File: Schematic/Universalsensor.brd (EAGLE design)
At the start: 62 x 62.2 mm, 26 parts, among them IC1 MEGA328P-AU, IC2 DS18B20, IC3 DHT-22, IC4 SHT1X, IC5 MAX1724

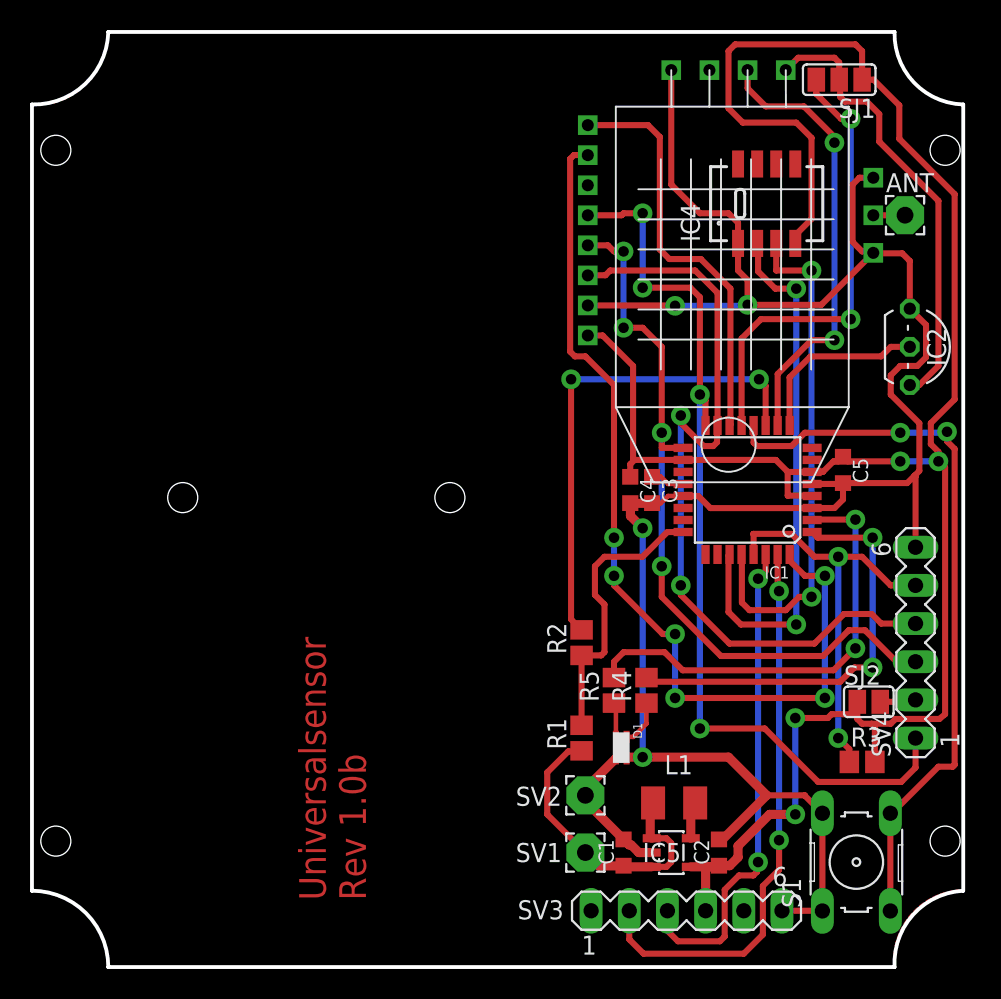
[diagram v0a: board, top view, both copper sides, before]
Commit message: new schematic for low freq crystal oscillator and sht21
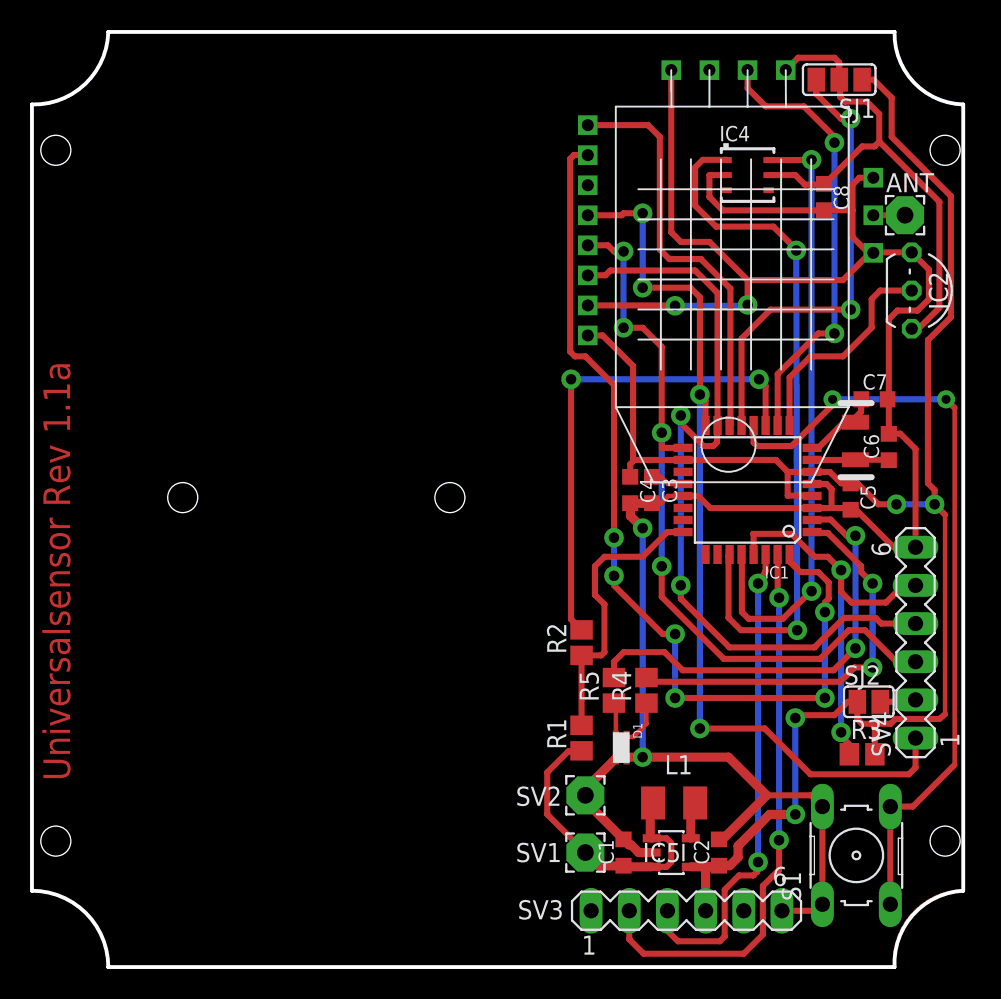
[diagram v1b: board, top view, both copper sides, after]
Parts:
- added C6, C7: 22pF, rcl:C0603K
- added C8: 100nF, rcl:C0603K
- added Q1: 32,768KHz, kanflo:OSCILLATOR_SMD
- IC4: value SHT1X -> SHT21; device sht10_11_15:SHT1X -> sensirion:DFN6/SHT
- moved IC2 3.75 mm to (58.5, 45.0)
- moved IC4 2.29 mm to (47.6, 52.7), turned to 270 degrees
- moved C5 1.85 mm to (54.5, 31.3)
- moved R3 0.51 mm to (55.2, 14.2)
- moved S1 0.44 mm to (54.9, 7.43)
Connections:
- new net N$3: C6.1, IC1.7, Q1.2
- new net N$8: C7.1, IC1.8, Q1.1
- net +3V3: no longer IC4.4
- net GND: now also C6.2, C7.2, C8.2, IC4.2; no longer IC4.1
- net SCL: now also IC4.6; no longer IC4.3
- net SDA: now also IC4.1; no longer IC4.2
- net U-SENS: now also C8.1, IC4.5
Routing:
- net +3V3: track 143.4 -> 114.4 mm
- net GND: track 149.9 -> 162.8 mm
- net SDA: track 36.0 -> 47.3 mm
- net SCL: track 34.3 -> 41.0 mm
- net N$8: track 0.00 -> 5.28 mm
- net N$3: track 0.00 -> 5.12 mm
- net U-SENS: track 30.2 -> 35.2 mm
- net D8: track 49.0 -> 52.0 mm
- net D5: track 12.0 -> 14.8 mm
- net D3: track 28.5 -> 27.0 mm
- net D4: track 30.0 -> 29.3 mm
- net !RES: track 27.6 -> 28.1 mm
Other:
- board text added: "Universalsensor Rev 1.1a"
- board text removed: "Universalsensor Rev 1.0b"

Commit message: schematic changed - only one crystal load capacitor needed, crystal doc added
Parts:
- C6, C7: value 22pF -> 10pF
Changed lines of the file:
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@@
 </attributes>
 <variantdefs>
-<variantdef name="DHT-22"/>
-<variantdef name="SHT-11"/>
+<variantdef name="DHT-22" current="yes"/>
+<variantdef name="SHT-21"/>
 </variantdefs>
 <classes>
@@
 </element>
 <element name="IC3" library="Pn-Lib" package="DHT-22-L" value="DHT-22" x="46.355" y="48.26" rot="R180">
-<variant name="SHT-11" populate="no"/>
+<variant name="SHT-21" populate="no"/>
 </element>
 <element name="SJ1" library="jumper" package="SJ_2" value="" x="53.721" y="59.055" rot="R180"/>
@@
 <element name="SJ2" library="jumper" package="SJ" value="" x="55.6895" y="17.653"/>
 <element name="Q1" library="kanflo" package="OSCILLATOR_SMD" value="32,768KHz" x="54.8005" y="36.2585" rot="R270"/>
-<element name="C6" library="rcl" package="C0603K" value="22pF" x="57.023" y="34.6075" rot="R90"/>
-<element name="C7" library="rcl" package="C0603K" value="22pF" x="56.0705" y="37.7825"/>
-<element name="IC4" library="sensirion" package="DFN6/SHT" value="SHT21" x="47.625" y="52.705" rot="R270"/>
+<element name="C6" library="rcl" package="C0603K" value="10pF" x="57.023" y="34.6075" rot="R90">
+<variant name="DHT-22" populate="no"/>
+<variant name="SHT-21" populate="no"/>
+</element>
+<element name="C7" library="rcl" package="C0603K" value="10pF" x="56.0705" y="37.7825"/>
+<element name="IC4" library="sensirion" package="DFN6/SHT" value="SHT21" x="47.625" y="52.705" rot="R270">
+<variant name="DHT-22" populate="no"/>
+</element>
 <element name="C8" library="rcl" package="C0603K" value="100nF" x="52.705" y="51.2445" rot="R270"/>
 </elements>
@@
 </signal>
 </signals>
-<errors>
-</errors>
 </board>
 </drawing>
